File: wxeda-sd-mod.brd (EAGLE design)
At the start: 101.3 x 40.6 mm, 26 parts, among them T1 2N3904, U1 SD_CARD, X1 TV OUT, X2 TAPE IN / OUT

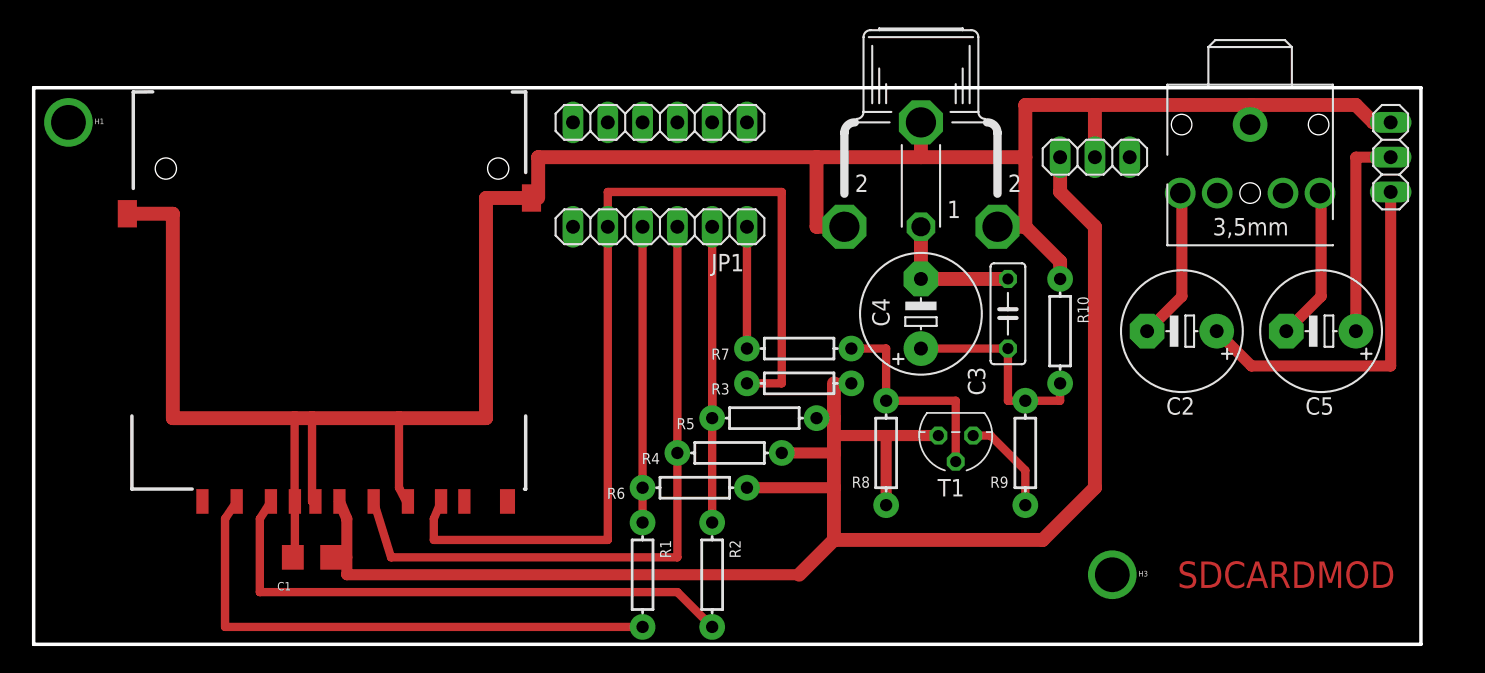
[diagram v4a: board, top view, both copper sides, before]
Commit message: Added S-Video connector against RCA
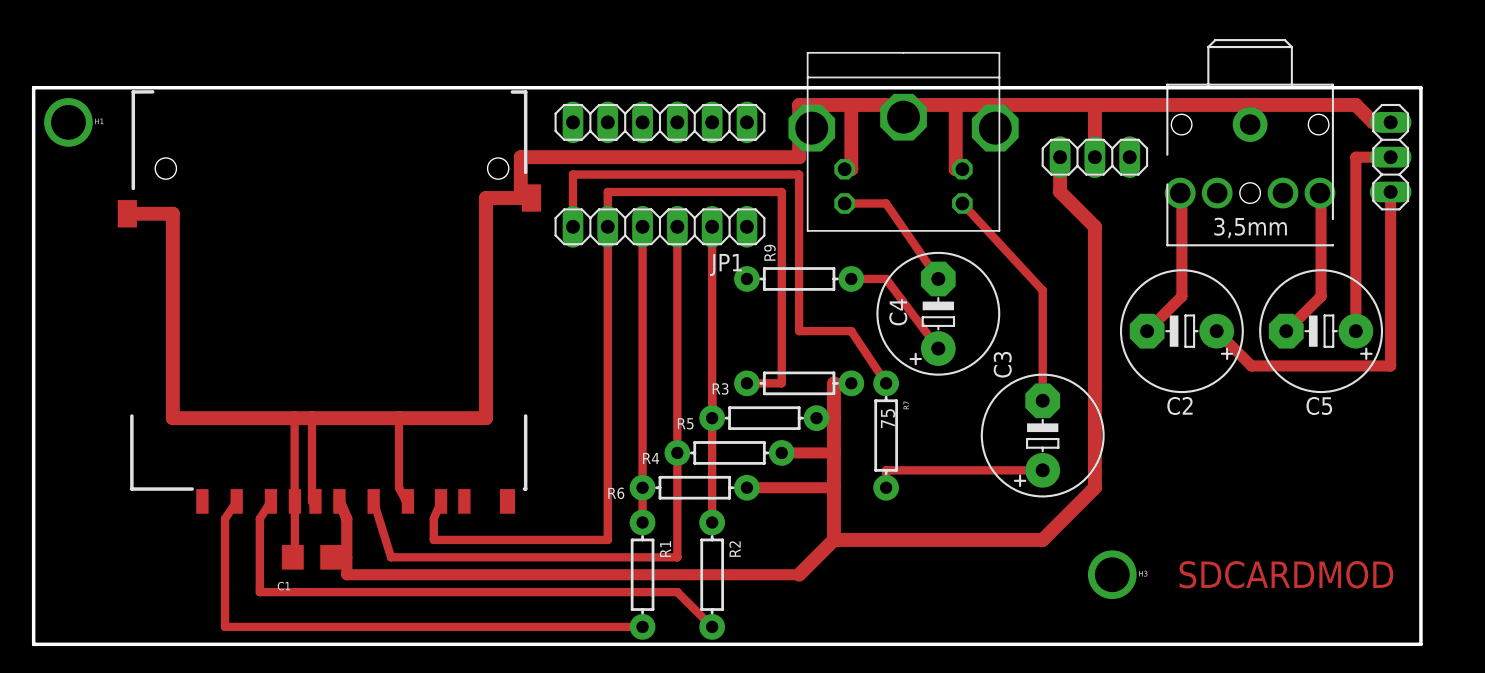
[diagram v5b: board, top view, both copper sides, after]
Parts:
- removed R10: 150, SparkFun-Passives:AXIAL-0.3
- removed R8: 1k, SparkFun-Passives:AXIAL-0.3
- removed T1: 2N3904, transistor:TO92
- removed X1: TV OUT, con-hirschmann:TOBU3
- added U$1: S-VIDEO, connectors-digital:MINIDIN_4_3GND
- C3: value 22n -> 47uF; device adafruit:C050-025X075 -> adafruit:E5-8,5
- R7: value 680 -> 75
- R9: value 51 -> 75
- moved R9 20.8 mm to (55.9, 26.7), turned to 0 degrees
- moved C3 9.25 mm to (73.7, 15.2)
- moved R7 8.98 mm to (62.2, 15.2), turned to 270 degrees
- moved C4 1.27 mm to (66.0, 24.1)
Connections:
- removed net N$2: R7.P$2, R8.P$1, T1.2
- removed net TVOUT: C3.2, C4.-, X1.1
- new net C_OUT: C4.-, U$1.4
- new net Y_OUT: C3.-, U$1.3
- net DSE: now also R7.P$1
- net DSEN4: now also R9.P$1; no longer R7.P$1
- net GND: now also U$1.1, U$1.2, U$1.CASE1, U$1.CASE2, U$1.SHIELDING; no longer R10.P$1, X1.2, X1.2@1, X1.2@2
- net N$7: now also C4.+, R9.P$2; no longer R9.P$1, T1.3
- net N$8: now also C3.+, R7.P$2; no longer C3.1, C4.+, R10.P$2, R9.P$2
- net VCC: no longer R8.P$2, T1.1
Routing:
- net DSE: track 0.00 -> 40.1 mm
- net Y_OUT: track 0.00 -> 16.7 mm
- net N$2: track 15.9 -> 0.00 mm
- net VCC: track 125.9 -> 113.2 mm
- net TVOUT: track 10.2 -> 0.00 mm
- net C_OUT: track 0.00 -> 9.73 mm
- net DSEN4: track 8.89 -> 0.00 mm
- net GND: track 180.9 -> 175.4 mm
- net N$8: track 15.2 -> 12.7 mm
- net N$7: track 7.40 -> 8.89 mm
